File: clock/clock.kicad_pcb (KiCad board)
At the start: 2 copper layers, 100 x 50 mm, 13 parts, among them J1 SWD, U1 iv12, U2 iv12, U3 iv12, U4 iv12, U5 STM32F103C8Tx, Y1 8Mhz, Y2 32.768khz

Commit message: Start of power design
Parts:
- added C5: 104, Capacitors_SMD:C_0603_HandSoldering, B.Cu at (121.0, 111.0)
- added C6: 104, Capacitors_SMD:C_0603_HandSoldering, B.Cu at (133.0, 113.0)
- added C7: 104, Capacitors_SMD:C_0603_HandSoldering, B.Cu at (129.0, 105.0)
- added C8: 104, Capacitors_SMD:C_0603_HandSoldering, B.Cu at (125.0, 117.0)
- added C9: 104, Capacitors_SMD:C_0603_HandSoldering, B.Cu at (153.0, 108.0)
- added J2: Barrel_Jack, Connectors:Barrel_Jack_CUI_PJ-036AH-SMT, B.Cu at (168.0, 111.0)
- moved J1 3.42 mm to (149.0, 105.0)
- moved U2 2.03 mm to (111.0, 127.0)
- moved U3 2.03 mm to (143.0, 127.0)
- moved U1 1.90 mm to (87.0, 127.0)
- moved U4 1.90 mm to (167.0, 127.0)
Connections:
- net Net-(J1-Pad2) renamed SWDIO
- net Net-(J1-Pad3) renamed SWCLK
- U1 pad 1: Net-(U1-Pad1) -> (no net)
- U1 pad 10: Net-(U1-Pad10) -> (no net)
- U1 pad 5: Net-(U1-Pad5) -> (no net)
- U1 pad 6: Net-(U1-Pad6) -> (no net)
- U1 pad 7: Net-(U1-Pad7) -> (no net)
- U1 pad 8: Net-(U1-Pad8) -> (no net)
- U1 pad 9: Net-(U1-Pad9) -> (no net)
- U2 pad 1: Net-(U2-Pad1) -> (no net)
- U2 pad 10: Net-(U2-Pad10) -> (no net)
- U2 pad 5: Net-(U2-Pad5) -> (no net)
- U2 pad 6: Net-(U2-Pad6) -> (no net)
- U2 pad 7: Net-(U2-Pad7) -> (no net)
- U2 pad 8: Net-(U2-Pad8) -> (no net)
- U2 pad 9: Net-(U2-Pad9) -> (no net)
- U3 pad 1: Net-(U3-Pad1) -> (no net)
- U3 pad 10: Net-(U3-Pad10) -> (no net)
- U3 pad 5: Net-(U3-Pad5) -> (no net)
- U3 pad 6: Net-(U3-Pad6) -> (no net)
- U3 pad 7: Net-(U3-Pad7) -> (no net)
- U3 pad 8: Net-(U3-Pad8) -> (no net)
- U3 pad 9: Net-(U3-Pad9) -> (no net)
- U4 pad 1: Net-(U4-Pad1) -> (no net)
- U4 pad 10: Net-(U4-Pad10) -> (no net)
- U4 pad 5: Net-(U4-Pad5) -> (no net)
- U4 pad 6: Net-(U4-Pad6) -> (no net)
- U4 pad 7: Net-(U4-Pad7) -> (no net)
- U4 pad 8: Net-(U4-Pad8) -> (no net)
- U4 pad 9: Net-(U4-Pad9) -> (no net)
- U5 pad 10: (no net) -> Net-(U5-Pad10)
- U5 pad 11: (no net) -> Net-(U5-Pad11)
- U5 pad 12: (no net) -> Net-(U5-Pad12)
- U5 pad 13: (no net) -> Net-(U5-Pad13)
- U5 pad 14: (no net) -> Net-(U5-Pad14)
- U5 pad 15: (no net) -> Net-(U5-Pad15)
- U5 pad 16: (no net) -> Net-(U5-Pad16)
- U5 pad 17: (no net) -> Net-(U5-Pad17)
- U5 pad 18: (no net) -> Net-(U5-Pad18)
- U5 pad 19: (no net) -> Net-(U5-Pad19)
- U5 pad 2: (no net) -> Net-(U5-Pad2)
- U5 pad 20: (no net) -> Net-(U5-Pad20)
- U5 pad 21: (no net) -> Net-(U5-Pad21)
- U5 pad 22: (no net) -> Net-(U5-Pad22)
- U5 pad 25: (no net) -> Net-(U5-Pad25)
- U5 pad 26: (no net) -> Net-(U5-Pad26)
- U5 pad 27: (no net) -> Net-(U5-Pad27)
- U5 pad 28: (no net) -> Net-(U5-Pad28)
- U5 pad 29: (no net) -> Net-(U5-Pad29)
- U5 pad 30: (no net) -> Net-(U5-Pad30)
- U5 pad 31: (no net) -> Net-(U5-Pad31)
- U5 pad 32: (no net) -> Net-(U5-Pad32)
- U5 pad 33: (no net) -> Net-(U5-Pad33)
- U5 pad 38: (no net) -> Net-(U5-Pad38)
- U5 pad 39: (no net) -> Net-(U5-Pad39)
- U5 pad 40: (no net) -> Net-(U5-Pad40)
- U5 pad 41: (no net) -> Net-(U5-Pad41)
- U5 pad 42: (no net) -> Net-(U5-Pad42)
- U5 pad 43: (no net) -> Net-(U5-Pad43)
- U5 pad 44: (no net) -> Net-(U5-Pad44)
- U5 pad 45: (no net) -> Net-(U5-Pad45)
- U5 pad 46: (no net) -> Net-(U5-Pad46)
- U5 pad 7: (no net) -> Net-(U5-Pad7)
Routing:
- added copper zone on B.Cu, net GND

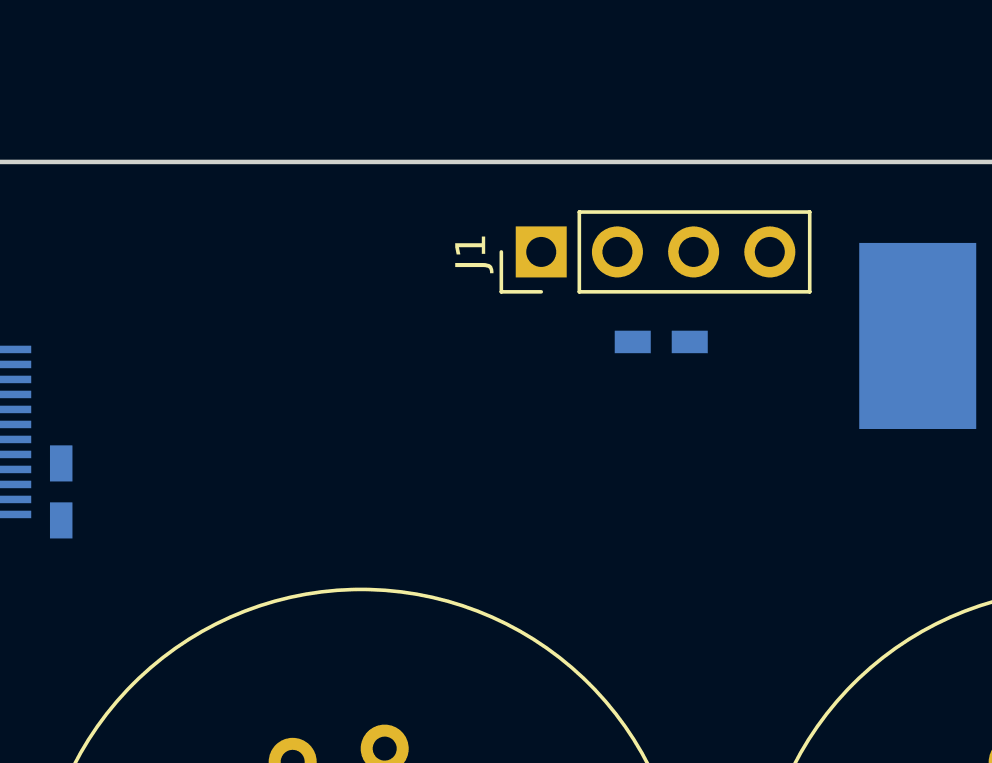
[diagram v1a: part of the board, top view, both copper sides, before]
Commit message: Moved around power features
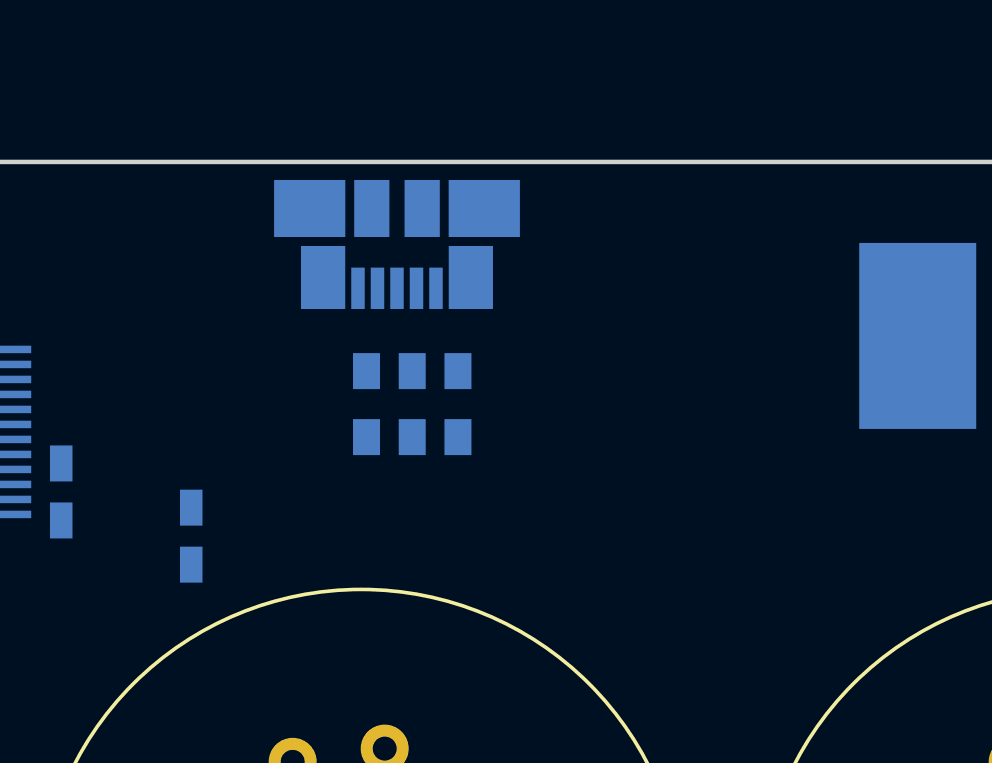
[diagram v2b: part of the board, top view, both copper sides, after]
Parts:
- added R1: 22R, Resistors_SMD:R_0603_HandSoldering, B.Cu at (144.7, 110.1)
- added R2: 22R, Resistors_SMD:R_0603_HandSoldering, B.Cu at (143.2, 110.1)
- added R3: 10k, Resistors_SMD:R_0603_HandSoldering, B.Cu at (146.2, 110.1)
- J1: value SWD -> USB_OTG; footprint Pin_Headers:Pin_Header_Straight_1x04_Pitch2.54mm -> Connectors_USB:USB_Micro-B_Molex_47346-0001; moved to B.Cu
- moved C9 17.0 mm to (137.3, 114.5), turned to 90 degrees
- moved J1 5.02 mm to (144.2, 103.6), turned to 0 degrees
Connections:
- J1 pad 1: +3V3 -> +5V
- J1 pad 2: SWDIO -> Net-(J1-Pad2)
- J1 pad 3: SWCLK -> Net-(J1-Pad3)
- J2 pad 1: +VDC -> (no net)
- U5 pad 10: Net-(U5-Pad10) -> (no net)
- U5 pad 11: Net-(U5-Pad11) -> (no net)
- U5 pad 12: Net-(U5-Pad12) -> (no net)
- U5 pad 13: Net-(U5-Pad13) -> (no net)
- U5 pad 14: Net-(U5-Pad14) -> (no net)
- U5 pad 15: Net-(U5-Pad15) -> (no net)
- U5 pad 16: Net-(U5-Pad16) -> (no net)
- U5 pad 17: Net-(U5-Pad17) -> (no net)
- U5 pad 18: Net-(U5-Pad18) -> (no net)
- U5 pad 19: Net-(U5-Pad19) -> (no net)
- U5 pad 2: Net-(U5-Pad2) -> (no net)
- U5 pad 20: Net-(U5-Pad20) -> (no net)
- U5 pad 21: Net-(U5-Pad21) -> (no net)
- U5 pad 22: Net-(U5-Pad22) -> (no net)
- U5 pad 25: Net-(U5-Pad25) -> (no net)
- U5 pad 26: Net-(U5-Pad26) -> (no net)
- U5 pad 27: Net-(U5-Pad27) -> (no net)
- U5 pad 28: Net-(U5-Pad28) -> (no net)
- U5 pad 29: Net-(U5-Pad29) -> (no net)
- U5 pad 30: Net-(U5-Pad30) -> (no net)
- U5 pad 31: Net-(U5-Pad31) -> (no net)
- U5 pad 32: Net-(U5-Pad32) -> D-
- U5 pad 33: Net-(U5-Pad33) -> D+
- U5 pad 34: SWDIO -> (no net)
- U5 pad 37: SWCLK -> (no net)
- U5 pad 38: Net-(U5-Pad38) -> (no net)
- U5 pad 39: Net-(U5-Pad39) -> (no net)
- U5 pad 40: Net-(U5-Pad40) -> (no net)
- U5 pad 41: Net-(U5-Pad41) -> (no net)
- U5 pad 42: Net-(U5-Pad42) -> (no net)
- U5 pad 43: Net-(U5-Pad43) -> (no net)
- U5 pad 44: Net-(U5-Pad44) -> (no net)
- U5 pad 45: Net-(U5-Pad45) -> (no net)
- U5 pad 46: Net-(U5-Pad46) -> (no net)
- U5 pad 7: Net-(U5-Pad7) -> (no net)

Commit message: Rev 1 of clock display board
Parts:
- removed BT1: Battery_Cell, Battery_Holders:Keystone_3000_1x12mm-CoinCell
- removed C1, C2, C3, C4: 20p, Capacitors_SMD:C_0603_HandSoldering
- removed C5, C6, C7, C8, C9: 104, Capacitors_SMD:C_0603_HandSoldering
- removed Y1: 8Mhz, Crystals:Crystal_SMD_5032-2pin_5.0x3.2mm
- removed Y2: 32.768khz, Crystals:Crystal_SMD_3215-2pin_3.2x1.5mm
- added J3: 5v, Connector_PinHeader_2.54mm:PinHeader_1x01_P2.54mm_Vertical, B.Cu at (103.3, 111.7)
- added J4: Conn_01x01_Male, Connector_PinHeader_2.54mm:PinHeader_1x01_P2.54mm_Vertical, B.Cu at (95.6, 111.7)
- added J5: 24v, Connector_PinHeader_2.54mm:PinHeader_1x01_P2.54mm_Vertical, B.Cu at (103.3, 142.2)
- added J6: Conn_01x01_Male, Connector_PinHeader_2.54mm:PinHeader_1x01_P2.54mm_Vertical, B.Cu at (95.6, 142.2)
- added R10: 10k, Resistor_SMD:R_0603_1608Metric_Pad1.05x0.95mm_HandSolder, F.Cu at (90.6, 111.5)
- added R11: 10k, Resistor_SMD:R_0603_1608Metric_Pad1.05x0.95mm_HandSolder, F.Cu at (145.4, 111.3)
- added R12: 10k, Resistor_SMD:R_0603_1608Metric_Pad1.05x0.95mm_HandSolder, F.Cu at (169.8, 111.5)
- added R13: 10k, Resistor_SMD:R_0603_1608Metric_Pad1.05x0.95mm_HandSolder, F.Cu at (115.8, 111.5)
- added R14: 10k, Resistor_SMD:R_0603_1608Metric_Pad1.05x0.95mm_HandSolder, F.Cu at (92.1, 111.5)
- added R15: 10k, Resistor_SMD:R_0603_1608Metric_Pad1.05x0.95mm_HandSolder, F.Cu at (146.9, 111.3)
- added R16: 10k, Resistor_SMD:R_0603_1608Metric_Pad1.05x0.95mm_HandSolder, F.Cu at (171.3, 111.5)
- added R17: 10k, Resistor_SMD:R_0603_1608Metric_Pad1.05x0.95mm_HandSolder, F.Cu at (106.8, 111.5)
- added R18: 10k, Resistor_SMD:R_0603_1608Metric_Pad1.05x0.95mm_HandSolder, F.Cu at (83.1, 111.5)
- added R19: 10k, Resistor_SMD:R_0603_1608Metric_Pad1.05x0.95mm_HandSolder, F.Cu at (137.9, 111.3)
- added R20: 10k, Resistor_SMD:R_0603_1608Metric_Pad1.05x0.95mm_HandSolder, F.Cu at (162.3, 111.5)
- added R21: 10k, Resistor_SMD:R_0603_1608Metric_Pad1.05x0.95mm_HandSolder, F.Cu at (108.3, 111.5)
- added R22: 10k, Resistor_SMD:R_0603_1608Metric_Pad1.05x0.95mm_HandSolder, F.Cu at (84.6, 111.5)
- added R23: 10k, Resistor_SMD:R_0603_1608Metric_Pad1.05x0.95mm_HandSolder, F.Cu at (139.4, 111.3)
- added R24: 10k, Resistor_SMD:R_0603_1608Metric_Pad1.05x0.95mm_HandSolder, F.Cu at (163.8, 111.5)
- added R25: 10k, Resistor_SMD:R_0603_1608Metric_Pad1.05x0.95mm_HandSolder, F.Cu at (109.8, 111.5)
- added R26: 10k, Resistor_SMD:R_0603_1608Metric_Pad1.05x0.95mm_HandSolder, F.Cu at (86.1, 111.5)
- added R27: 10k, Resistor_SMD:R_0603_1608Metric_Pad1.05x0.95mm_HandSolder, F.Cu at (140.9, 111.3)
- added R28: 10k, Resistor_SMD:R_0603_1608Metric_Pad1.05x0.95mm_HandSolder, F.Cu at (165.3, 111.5)
- added R29: R_Small, Resistor_SMD:R_0603_1608Metric_Pad1.05x0.95mm_HandSolder, B.Cu at (138.0, 111.3)
- added R30: R_Small, Resistor_SMD:R_0603_1608Metric_Pad1.05x0.95mm_HandSolder, B.Cu at (106.8, 111.5)
- added R31: R_Small, Resistor_SMD:R_0603_1608Metric_Pad1.05x0.95mm_HandSolder, B.Cu at (83.0, 111.5)
- added R32: R_Small, Resistor_SMD:R_0603_1608Metric_Pad1.05x0.95mm_HandSolder, B.Cu at (162.2, 111.5)
- added R4: 10k, Resistor_SMD:R_0603_1608Metric_Pad1.05x0.95mm_HandSolder, F.Cu at (166.8, 111.5)
- added R5: 10k, Resistor_SMD:R_0603_1608Metric_Pad1.05x0.95mm_HandSolder, F.Cu at (112.8, 111.5)
- added R6: 10k, Resistor_SMD:R_0603_1608Metric_Pad1.05x0.95mm_HandSolder, F.Cu at (89.1, 111.5)
- added R7: 10k, Resistor_SMD:R_0603_1608Metric_Pad1.05x0.95mm_HandSolder, F.Cu at (143.9, 111.3)
- added R8: 10k, Resistor_SMD:R_0603_1608Metric_Pad1.05x0.95mm_HandSolder, F.Cu at (168.3, 111.5)
- added R9: 10k, Resistor_SMD:R_0603_1608Metric_Pad1.05x0.95mm_HandSolder, F.Cu at (114.3, 111.5)
- added REF**: OSHW-Symbol_13.4x12mm_SilkScreen, Symbol:OSHW-Symbol_13.4x12mm_SilkScreen, B.Cu at (127.0, 127.0)
- added REF**: MountingHole_3.2mm_M3, MountingHole:MountingHole_3.2mm_M3, F.Cu at (102.5, 150.0)
- added REF**: MountingHole_3.2mm_M3, MountingHole:MountingHole_3.2mm_M3, F.Cu at (151.5, 150.0)
- added REF**: MountingHole_3.2mm_M3, MountingHole:MountingHole_3.2mm_M3, F.Cu at (102.5, 104.0)
- added REF**: MountingHole_3.2mm_M3, MountingHole:MountingHole_3.2mm_M3, F.Cu at (151.5, 104.0)
- added U6: ULN2003, Package_SO:SOIC-16_3.9x9.9mm_P1.27mm, B.Cu at (111.2, 139.8)
- added U7: ULN2003, Package_SO:SOIC-16_3.9x9.9mm_P1.27mm, B.Cu at (142.2, 139.8)
- added U8: ULN2003, Package_SO:SOIC-16_3.9x9.9mm_P1.27mm, B.Cu at (166.8, 139.8)
- J1: value USB_OTG -> Conn_01x16_Male; footprint Connectors_USB:USB_Micro-B_Molex_47346-0001 -> Connector_PinHeader_2.54mm:PinHeader_1x16_P2.54mm_Vertical
- J2: value Barrel_Jack -> Conn_01x16_Male; footprint Connectors:Barrel_Jack_CUI_PJ-036AH-SMT -> Connector_PinHeader_2.54mm:PinHeader_1x16_P2.54mm_Vertical
- R1, R2: value 22R -> 10k; footprint Resistors_SMD:R_0603_HandSoldering -> Resistor_SMD:R_0603_1608Metric_Pad1.05x0.95mm_HandSolder; moved to F.Cu
- R3: footprint Resistors_SMD:R_0603_HandSoldering -> Resistor_SMD:R_0603_1608Metric_Pad1.05x0.95mm_HandSolder; moved to F.Cu
- U1, U2, U3, U4: footprint tubes:iv12 -> tubes:iv12-large
- U5: value STM32F103C8Tx -> ULN2003; footprint Housings_QFP:LQFP-48_7x7mm_Pitch0.5mm -> Package_SO:SOIC-16_3.9x9.9mm_P1.27mm
- moved J2 60.5 mm to (108.0, 104.0), turned to 270 degrees
- moved R2 55.6 mm to (87.6, 111.5)
- moved U5 49.1 mm to (87.2, 139.8), turned to 90 degrees
- moved J1 46.5 mm to (146.1, 150.0), turned to 90 degrees
- moved R1 33.4 mm to (111.3, 111.5)
- moved R3 3.98 mm to (142.4, 111.3)
- moved U3 0.75 mm to (142.2, 127.0)
- moved U1 0.25 mm to (87.2, 127.0)
- moved U2 0.25 mm to (111.2, 127.0)
- moved U4 0.25 mm to (166.8, 127.0)
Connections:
- J1 pad 4: GND -> Net-(J1-Pad4)
- J1 pad 5: GND -> Net-(J1-Pad5)
- J1 pad 6: GND -> Net-(J1-Pad6)
- J2 pad 1: (no net) -> +5V
- J2 pad 2: GND -> Net-(J2-Pad2)
- J2 pad 3: GND -> Net-(J2-Pad3)
- R1 pad 1: Net-(J1-Pad3) -> +24V
- R1 pad 2: D+ -> Net-(R1-Pad2)
- R2 pad 1: Net-(J1-Pad2) -> +24V
- R2 pad 2: D- -> Net-(R2-Pad2)
- R3 pad 1: +5V -> +24V
- R3 pad 2: D+ -> Net-(R3-Pad2)
- U1 pad 1: (no net) -> Net-(R18-Pad2)
- U1 pad 10: (no net) -> Net-(R22-Pad2)
- U1 pad 3: +1V5 -> Net-(R31-Pad1)
- U1 pad 5: (no net) -> Net-(R14-Pad2)
- U1 pad 6: (no net) -> Net-(R10-Pad2)
- U1 pad 7: (no net) -> Net-(R6-Pad2)
- U1 pad 8: (no net) -> Net-(R2-Pad2)
- U1 pad 9: (no net) -> Net-(R26-Pad2)
- U2 pad 1: (no net) -> Net-(R17-Pad2)
- U2 pad 10: (no net) -> Net-(R21-Pad2)
- U2 pad 3: +1V5 -> Net-(R30-Pad1)
- U2 pad 5: (no net) -> Net-(R13-Pad2)
- U2 pad 6: (no net) -> Net-(R9-Pad2)
- U2 pad 7: (no net) -> Net-(R5-Pad2)
- U2 pad 8: (no net) -> Net-(R1-Pad2)
- U2 pad 9: (no net) -> Net-(R25-Pad2)
- U3 pad 1: (no net) -> Net-(R19-Pad2)
- U3 pad 10: (no net) -> Net-(R23-Pad2)
- U3 pad 3: +1V5 -> Net-(R29-Pad1)
- U3 pad 5: (no net) -> Net-(R15-Pad2)
- U3 pad 6: (no net) -> Net-(R11-Pad2)
- U3 pad 7: (no net) -> Net-(R7-Pad2)
- U3 pad 8: (no net) -> Net-(R3-Pad2)
- U3 pad 9: (no net) -> Net-(R27-Pad2)
- U4 pad 1: (no net) -> Net-(R20-Pad2)
- U4 pad 10: (no net) -> Net-(R24-Pad2)
- U4 pad 3: +1V5 -> Net-(R32-Pad1)
- U4 pad 5: (no net) -> Net-(R16-Pad2)
- U4 pad 6: (no net) -> Net-(R12-Pad2)
- U4 pad 7: (no net) -> Net-(R8-Pad2)
- U4 pad 8: (no net) -> Net-(R4-Pad2)
- U4 pad 9: (no net) -> Net-(R28-Pad2)
- U5 pad 1: VBAT -> Net-(J1-Pad9)
- U5 pad 10: (no net) -> Net-(R26-Pad2)
- U5 pad 11: (no net) -> Net-(R22-Pad2)
- U5 pad 12: (no net) -> Net-(R18-Pad2)
- U5 pad 13: (no net) -> Net-(R14-Pad2)
- U5 pad 14: (no net) -> Net-(R10-Pad2)
- U5 pad 15: (no net) -> Net-(R6-Pad2)
- U5 pad 16: (no net) -> Net-(R2-Pad2)
- U5 pad 2: (no net) -> Net-(J1-Pad10)
- U5 pad 3: Net-(C3-Pad1) -> Net-(J1-Pad11)
- U5 pad 4: Net-(C4-Pad1) -> Net-(J1-Pad12)
- U5 pad 5: Net-(C1-Pad1) -> Net-(J1-Pad13)
- U5 pad 6: Net-(C2-Pad1) -> Net-(J1-Pad14)
- U5 pad 7: (no net) -> Net-(J1-Pad15)
- U5 pad 9: +3V3 -> +24V
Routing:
- net +24V: track 0.00 -> 261.8 mm, vias 0 -> 4
- net +5V: track 0.00 -> 179.9 mm, vias 0 -> 2
- net Net-(J2-Pad9): track 0.00 -> 72.3 mm
- net Net-(J2-Pad10): track 0.00 -> 68.2 mm
- net Net-(J2-Pad2): track 0.00 -> 67.2 mm
- net Net-(J2-Pad11): track 0.00 -> 64.2 mm
- net Net-(J2-Pad3): track 0.00 -> 62.8 mm
- net Net-(J2-Pad12): track 0.00 -> 60.3 mm
- net Net-(J2-Pad4): track 0.00 -> 59.1 mm
- net Net-(J2-Pad13): track 0.00 -> 58.0 mm
- net Net-(J2-Pad5): track 0.00 -> 56.3 mm
- net Net-(J2-Pad14): track 0.00 -> 55.2 mm
- net Net-(J2-Pad6): track 0.00 -> 53.4 mm
- net Net-(J2-Pad15): track 0.00 -> 52.3 mm
- net Net-(J2-Pad7): track 0.00 -> 50.6 mm
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- added copper zone on F.Cu, net GND
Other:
- net class 24v added: clearance 0.152, trace_width 0.4, via_dia 0.6, via_drill 0.3
- net class 5v added: clearance 0.152, trace_width 0.4, via_dia 0.6, via_drill 0.3
- board text added: "IV-12 Clock Display Board https://github.com/Wiles/iv-12 Rev. 1"
- board text added: "MT3608"
